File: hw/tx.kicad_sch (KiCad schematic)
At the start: 61 parts, among them Q301 MMBF170, Q302 MMBF170, Q303 MMBF170, Q304 MMBF170, Q305 MMBF170, Q306 MMBF170, Q307 MMBF170, Q308 MMBF170, Q309 MMBF170, Q310 MMBF170, Q311 MMBF170, Q312 MMBF170, T301 BN-43-202_DualPri_CTSec, U301 ICE40UP5K-SG48ITR, U302 CD74ACT541SM96, Y301 40MHz

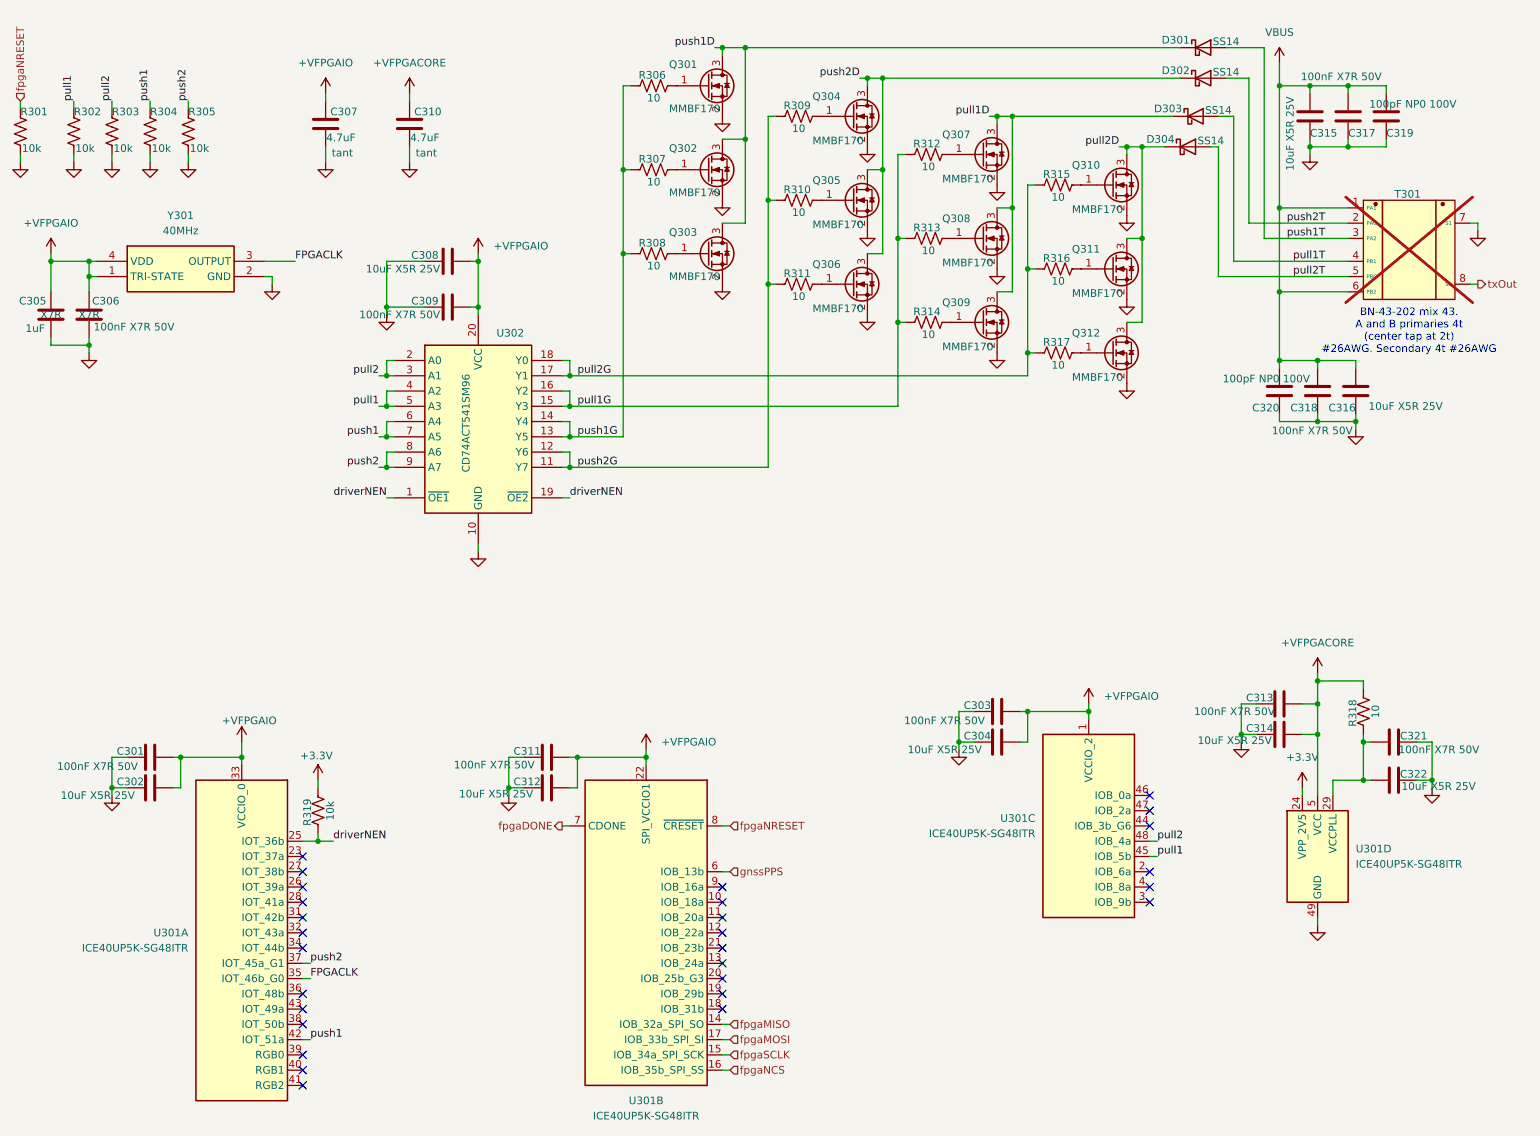
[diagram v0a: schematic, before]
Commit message: Separate FPGA config CRESET from software NRESET, add RGB heartbeat to FPGA.
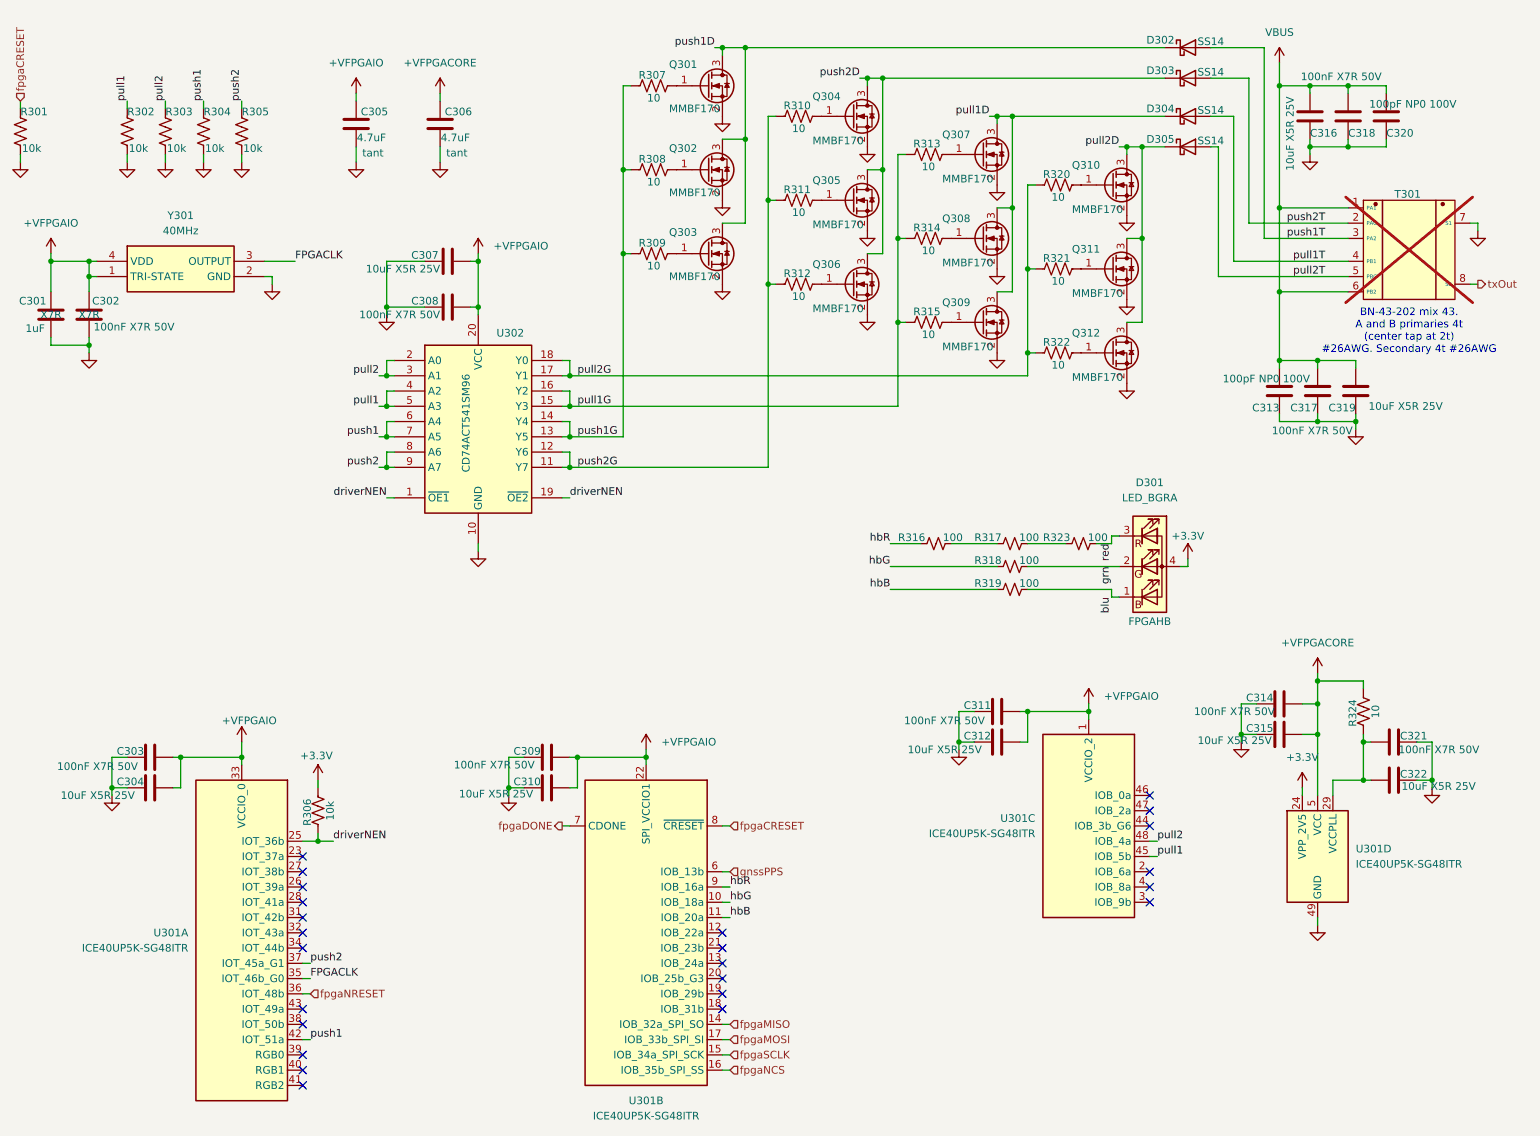
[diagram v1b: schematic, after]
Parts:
- added D301: LED_BGRA, Library:UHD111AFKAC3K23E1L3VG5ZB3Z3, symbol Device:LED_BGRA
- added R316, R317, R318, R319, R323: 100, Resistor_SMD:R_0402_1005Metric, symbol Device:R_Small_US
- renumbered C305 to C301, C306 to C302, C301 to C303, C302 to C304, C307 to C305, C310 to C306, C308 to C307, C309 to C308, C311 to C309, C312 to C310, C303 to C311, C304 to C312, C320 to C313, C313 to C314, C314 to C315, C315 to C316, C318 to C317, C317 to C318, C316 to C319, C319 to C320, D301 to D302, D302 to D303, D303 to D304, D304 to D305, R319 to R306, R306 to R307, R307 to R308, R308 to R309, R309 to R310, R310 to R311, R311 to R312, R312 to R313, R313 to R314, R314 to R315, R315 to R320, R316 to R321, R317 to R322, R318 to R324
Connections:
- net +3.3V: now also D301.4 (A)
- net fpgaNRESET: now also U301.36 (IOT_48b); no longer R301.1, U301.8 (~{CRESET})
- net hbG: now reaches U301.10 (IOB_18a)
- net hbG: now also R318.1
- net hbB: now reaches U301.11 (IOB_20a)
- net hbB: now also R319.1
- net hbR: now reaches U301.9 (IOB_16a)
- net hbR: now also R316.1
- new net: R317.2, R323.1
- new net: R316.2, R317.1
- new net blu: D301.1 (BK), R319.2
- new net fpgaCRESET: R301.1, U301.8 (~{CRESET})
- new net grn: D301.2 (GK), R318.2
- new net red: D301.3 (RK), R323.2
- no-connect marks 28 -> 24
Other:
- moved on the sheet: C305, C306, D302, D303, D304, R302, R303, R304, R305

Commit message: Move to single gate buffer per MOSFET to distribute decoupling and gate drive across more devices and improve gate drive signal quality at high speed
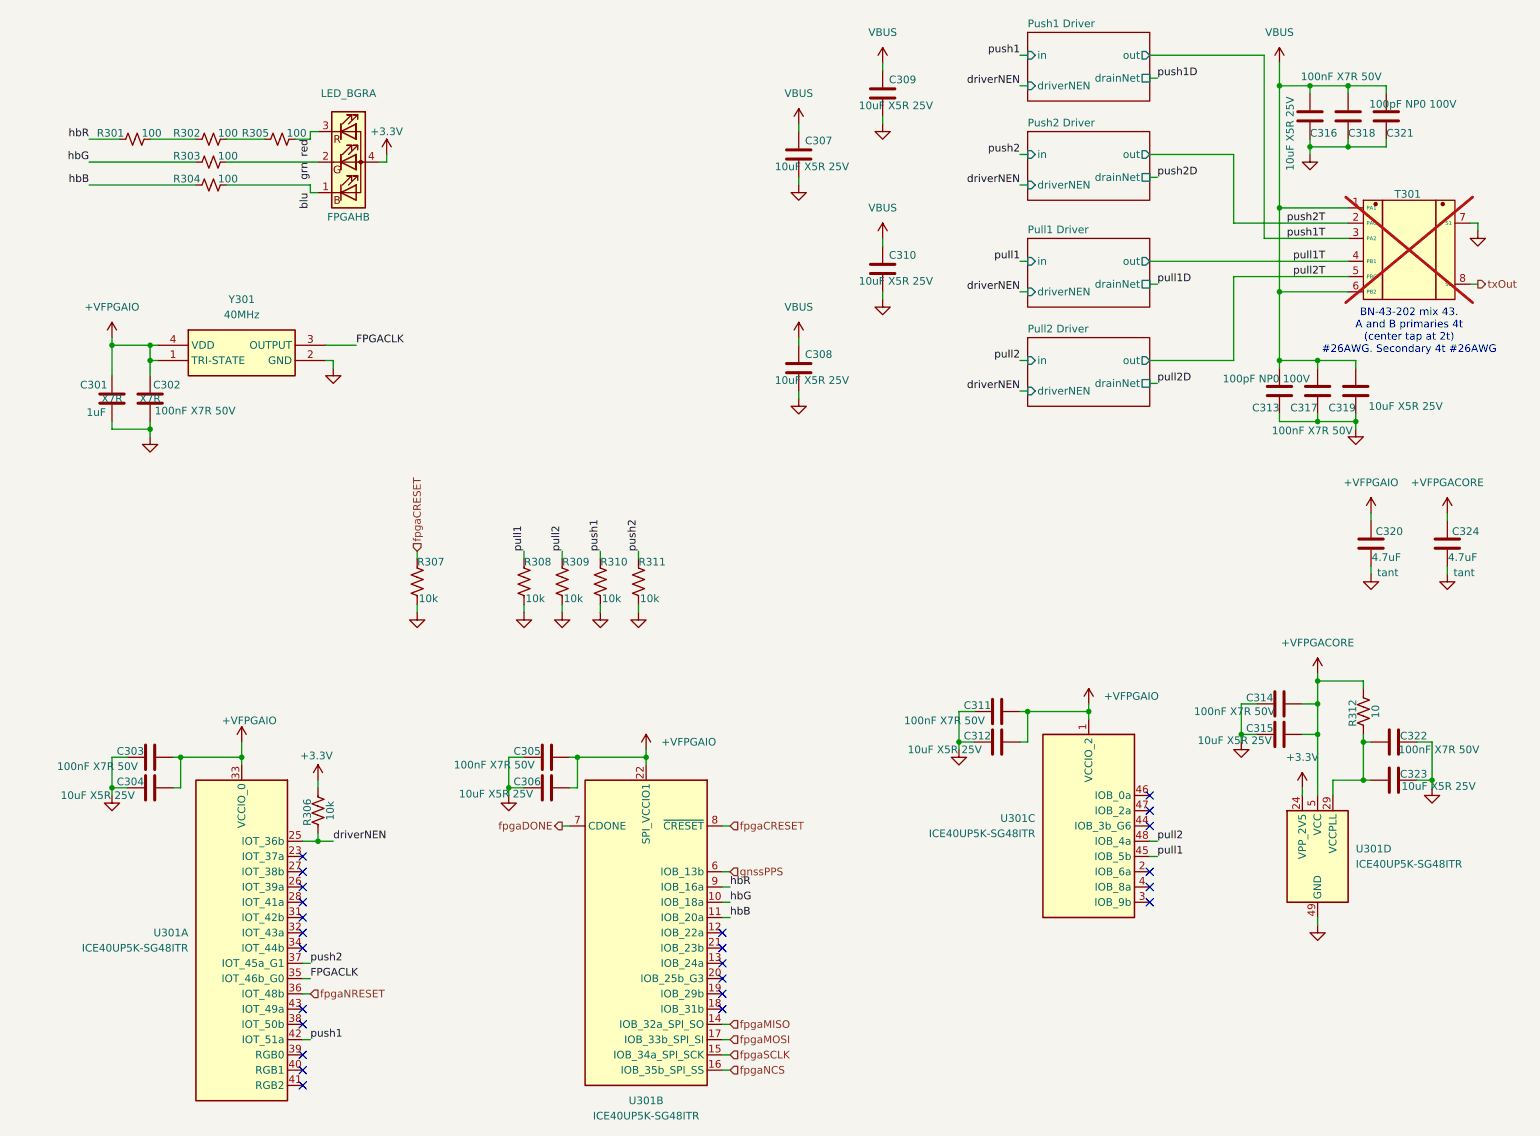
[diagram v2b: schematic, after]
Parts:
- removed D302, D303, D304, D305: SS14, Diode_SMD:D_SMA, symbol Diode:SS14
- removed Q301, Q302, Q303, Q304, Q305, Q306, Q307, Q308, Q309, Q310, Q311, Q312: MMBF170, Package_TO_SOT_SMD:SOT-23, symbol Transistor_FET:BS170F
- removed R307, R308, R309, R310, R311, R312, R313, R314, R315, R320, R321, R322: 10, Resistor_SMD:R_0603_1608Metric, symbol Device:R_US
- removed U302: CD74ACT541SM96, Library:SOP65P780X200-20N, symbol Library:CD74ACT541M96G4
- added C309, C310: 10uF X5R 25V, Capacitor_SMD:C_0603_1608Metric, symbol Device:C
- C308: value 100nF X7R 50V -> 10uF X5R 25V; LCSC C24452 -> C96446; MPN KGM15BR71H104KT -> CM105X5R106M25AT; Mouser_PN 581-KGM15BR71H104KT -> 346-CM105X5R106M25AT
- renumbered C309 to C305, C310 to C306, C305 to C320, C320 to C321, C321 to C322, C322 to C323, C306 to C324, R316 to R301, R317 to R302, R318 to R303, R319 to R304, R323 to R305, R301 to R307, R302 to R308, R303 to R309, R304 to R310, R305 to R311, R324 to R312
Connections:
- net +VFPGAIO: no longer C307.2, C308.2
- net GND: now also C309.1, C310.1
- net VBUS: now also C307.2, C308.2, C309.2, C310.2
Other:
- added sheet Pull1 Driver (phase-driver.kicad_sch)
- added sheet Pull2 Driver (phase-driver.kicad_sch)
- added sheet Push1 Driver (phase-driver.kicad_sch)
- added sheet Push2 Driver (phase-driver.kicad_sch)
- moved on the sheet: C301, C302, C320, C324, R301, R302, R303, R304, R305, R307, R308, R309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
